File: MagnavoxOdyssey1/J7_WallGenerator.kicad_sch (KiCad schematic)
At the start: 19 parts

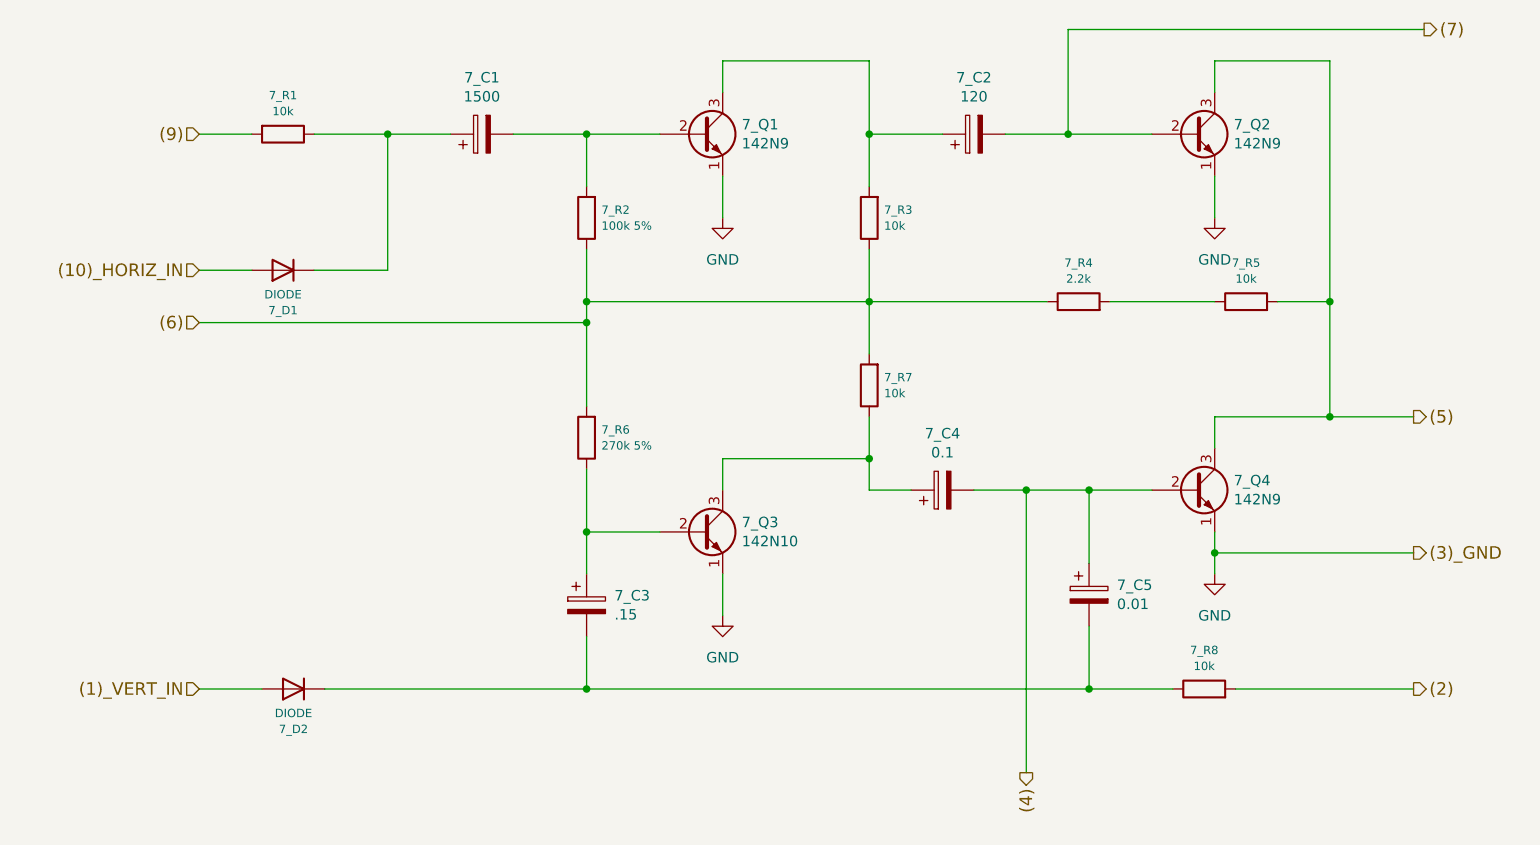
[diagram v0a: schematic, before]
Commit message: update to kicad 9
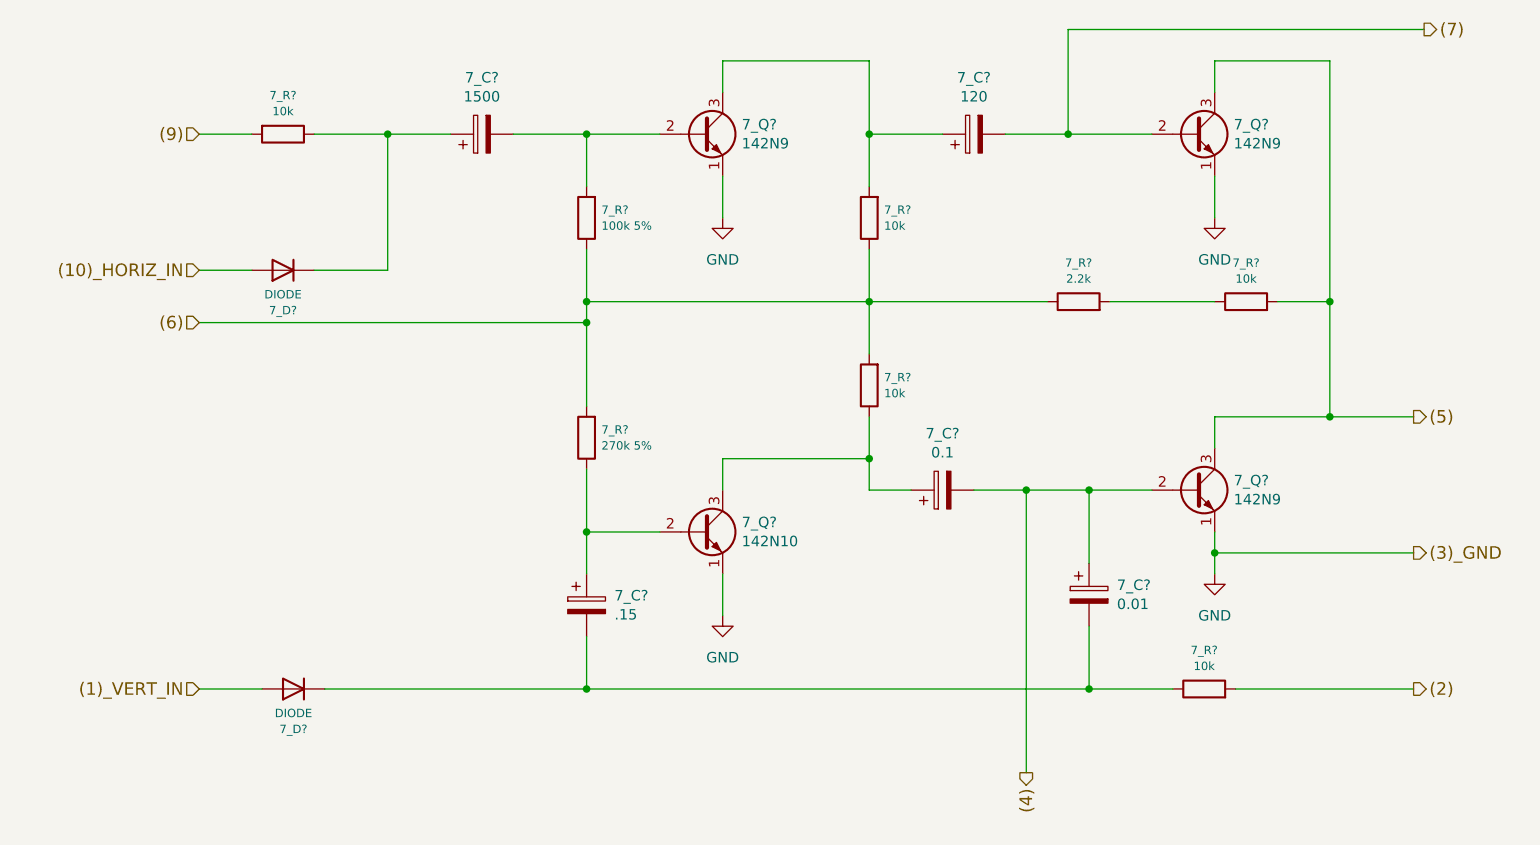
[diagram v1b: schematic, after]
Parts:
- 7_Q?: renamed from 7_Q1; symbol Device:Q_NPN_EBC -> Transistor_BJT:Q_NPN_EBC
- 7_Q?: renamed from 7_Q2; symbol Device:Q_NPN_EBC -> Transistor_BJT:Q_NPN_EBC
- 7_Q?: renamed from 7_Q3; symbol Device:Q_NPN_EBC -> Transistor_BJT:Q_NPN_EBC
- 7_Q?: renamed from 7_Q4; symbol Device:Q_NPN_EBC -> Transistor_BJT:Q_NPN_EBC
- renumbered 7_C1 to 7_C?, 7_C2 to 7_C?, 7_C4 to 7_C?, 7_C5 to 7_C?, 7_C3 to 7_C?, 7_D1 to 7_D?, 7_D2 to 7_D?, 7_R1 to 7_R?, 7_R2 to 7_R?, 7_R3 to 7_R?, 7_R6 to 7_R?, 7_R7 to 7_R?, 7_R8 to 7_R?, 7_R4 to 7_R?, 7_R5 to 7_R?
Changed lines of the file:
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@@
 (kicad_sch
-	(version 20231120)
+	(version 20250114)
 	(generator "eeschema")
-	(generator_version "8.0")
+	(generator_version "9.0")
 	(paper "A4")
 	(junction
@@
 		(on_board yes)
 		(dnp no)
-		(property "Reference" "7_D1"
+		(property "Reference" "7_D?"
 			(at 88.9 84.8868 0)
 			(effects
@@
 		)
 		(pin "1"
+		)
+		(instances
+			(project "MagnavoxOdyssey1"
+				(path "/adb6e295-eae5-402e-a614-02a705c3e27c/00000000-0000-0000-0000-0000588dc7ec"
+					(reference "7_D?")
+					(unit 1)
+				)
+			)
 		)
 	)
@@
 		(on_board yes)
 		(dnp no)
-		(property "Reference" "7_R1"
+		(property "Reference" "7_R?"
 			(at 88.9 58.801 90)
 			(effects
@@
 		)
 		(pin "1"
+		)
+		(instances
+			(project "MagnavoxOdyssey1"
+				(path "/adb6e295-eae5-402e-a614-02a705c3e27c/00000000-0000-0000-0000-0000588dc7ec"
+					(reference "7_R?")
+					(unit 1)
+				)
+			)
 		)
 	)
@@
 		(on_board yes)
 		(dnp no)
-		(property "Reference" "7_C1"
+		(property "Reference" "7_C?"
 			(at 113.03 56.642 90)
 			(effects
@@
 		)
 		(pin "2"
+		)
+		(instances
+			(project "MagnavoxOdyssey1"
+				(path "/adb6e295-eae5-402e-a614-02a705c3e27c/00000000-0000-0000-0000-0000588dc7ec"
+					(reference "7_C?")
+					(unit 1)
+				)
+			)
 		)
 	)
@@
 		(on_board yes)
 		(dnp no)
-		(property "Reference" "7_R2"
+		(property "Reference" "7_R?"
 			(at 127.5334 72.6948 0)
 			(effects
@@
 		(pin "1"
 		)
+		(instances
+			(project "MagnavoxOdyssey1"
+				(path "/adb6e295-eae5-402e-a614-02a705c3e27c/00000000-0000-0000-0000-0000588dc7ec"
+					(reference "7_R?")
+					(unit 1)
+				)
+			)
+		)
 	)
 	(symbol
-		(lib_id "Device:Q_NPN_EBC")
+		(lib_id "Transistor_BJT:Q_NPN_EBC")
 		(at 139.7 63.5 0)
 		(unit 1)
@@
 		(on_board yes)
 		(dnp no)
-		(property "Reference" "7_Q1"
+		(property "Reference" "7_Q?"
 			(at 144.5514 62.3316 0)
 			(effects
@@
 		)
 		(pin "3"
+		)
+		(instances
+			(project "MagnavoxOdyssey1"
+				(path "/adb6e295-eae5-402e-a614-02a705c3e27c/00000000-0000-0000-0000-0000588dc7ec"
+					(reference "7_Q?")
+					(unit 1)
+				)
+			)
 		)
 	)
@@
 		(on_board yes)
 		(dnp no)
-		(property "Reference" "7_R3"
+		(property "Reference" "7_R?"
 			(at 161.8234 72.6948 0)
 			(effects
@@
 		)
 		(pin "2"
+		)
+		(instances
+			(project "MagnavoxOdyssey1"
+				(path "/adb6e295-eae5-402e-a614-02a705c3e27c/00000000-0000-0000-0000-0000588dc7ec"
+					(reference "7_R?")
+					(unit 1)
+				)
+			)
 		)
 	)
@@
 		(on_board yes)
 		(dnp no)
-		(property "Reference" "7_C2"
+		(property "Reference" "7_C?"
 			(at 172.72 56.642 90)
 			(effects
@@
 		(pin "2"
 		)
+		(instances
+			(project "MagnavoxOdyssey1"
+				(path "/adb6e295-eae5-402e-a614-02a705c3e27c/00000000-0000-0000-0000-0000588dc7ec"
+					(reference "7_C?")
+					(unit 1)
+				)
+			)
+		)
 	)
 	(symbol
-		(lib_id "Device:Q_NPN_EBC")
+		(lib_id "Transistor_BJT:Q_NPN_EBC")
 		(at 199.39 63.5 0)
 		(unit 1)
@@
 		(on_board yes)
 		(dnp no)
-		(property "Reference" "7_Q2"
+		(property "Reference" "7_Q?"
 			(at 204.2414 62.3316 0)
 			(effects
@@
 		)
 		(pin "3"
+		)
+		(instances
+			(project "MagnavoxOdyssey1"
+				(path "/adb6e295-eae5-402e-a614-02a705c3e27c/00000000-0000-0000-0000-0000588dc7ec"
+					(reference "7_Q?")
+					(unit 1)
+				)
+			)
 		)
 	)
@@
 		(on_board yes)
 		(dnp no)
-		(property "Reference" "7_R6"
+		(property "Reference" "7_R?"
 			(at 127.5334 99.3648 0)
 			(effects
@@
 		(pin "2"
 		)
+		(instances
+			(project "MagnavoxOdyssey1"
+				(path "/adb6e295-eae5-402e-a614-02a705c3e27c/00000000-0000-0000-0000-0000588dc7ec"
+					(reference "7_R?")
+					(unit 1)
+				)
+			)
+		)
 	)
 	(symbol
-		(lib_id "Device:Q_NPN_EBC")
+		(lib_id "Transistor_BJT:Q_NPN_EBC")
 		(at 139.7 111.76 0)
 		(unit 1)
@@
 		(on_board yes)
 		(dnp no)
-		(property "Reference" "7_Q3"
+		(property "Reference" "7_Q?"
 			(at 144.5514 110.5916 0)
 			(effects
@@
 		)
 		(pin "3"
+		)
+		(instances
+			(project "MagnavoxOdyssey1"
+				(path "/adb6e295-eae5-402e-a614-02a705c3e27c/00000000-0000-0000-0000-0000588dc7ec"
+					(reference "7_Q?")
+					(unit 1)
+				)
+			)
 		)
 	)
@@
 		(on_board yes)
 		(dnp no)
-		(property "Reference" "7_R7"
+		(property "Reference" "7_R?"
 			(at 161.8234 93.0148 0)
 			(effects
@@
 		)
 		(pin "2"
+		)
+		(instances
+			(project "MagnavoxOdyssey1"
+				(path "/adb6e295-eae5-402e-a614-02a705c3e27c/00000000-0000-0000-0000-0000588dc7ec"
+					(reference "7_R?")
+					(unit 1)
+				)
+			)
 		)
 	)
@@
 		(on_board yes)
 		(dnp no)
-		(property "Reference" "7_C4"
+		(property "Reference" "7_C?"
 			(at 168.91 99.822 90)
 			(effects
@@
 		)
 		(pin "2"
+		)
+		(instances
+			(project "MagnavoxOdyssey1"
+				(path "/adb6e295-eae5-402e-a614-02a705c3e27c/00000000-0000-0000-0000-0000588dc7ec"
+					(reference "7_C?")
+					(unit 1)
+				)
+			)
 		)
 	)
@@
 		(on_board yes)
 		(dnp no)
-		(property "Reference" "7_C5"
+		(property "Reference" "7_C?"
 			(at 190.0682 118.2116 0)
 			(effects
@@
 		)
 		(pin "2"
+		)
+		(instances
+			(project "MagnavoxOdyssey1"
+				(path "/adb6e295-eae5-402e-a614-02a705c3e27c/00000000-0000-0000-0000-0000588dc7ec"
+					(reference "7_C?")
+					(unit 1)
+				)
+			)
 		)
 	)
@@
 		(on_board yes)
 		(dnp no)
-		(property "Reference" "7_C3"
+		(property "Reference" "7_C?"
 			(at 129.1082 119.4816 0)
 			(effects
@@
 		)
 		(pin "2"
+		)
+		(instances
+			(project "MagnavoxOdyssey1"
+				(path "/adb6e295-eae5-402e-a614-02a705c3e27c/00000000-0000-0000-0000-0000588dc7ec"
+					(reference "7_C?")
+					(unit 1)
+				)
+			)
 		)
 	)
@@
 		(on_board yes)
 		(dnp no)
-		(property "Reference" "7_R8"
+		(property "Reference" "7_R?"
 			(at 200.66 126.111 90)
 			(effects
@@
 		(pin "2"
 		)
+		(instances
+			(project "MagnavoxOdyssey1"
+				(path "/adb6e295-eae5-402e-a614-02a705c3e27c/00000000-0000-0000-0000-0000588dc7ec"
+					(reference "7_R?")
+					(unit 1)
+				)
+			)
+		)
 	)
 	(symbol
-		(lib_id "Device:Q_NPN_EBC")
+		(lib_id "Transistor_BJT:Q_NPN_EBC")
 		(at 199.39 106.68 0)
 		(unit 1)
@@
 		(on_board yes)
 		(dnp no)
-		(property "Reference" "7_Q4"
+		(property "Reference" "7_Q?"
 			(at 204.2414 105.5116 0)
 			(effects
@@
 		)
 		(pin "3"
+		)
+		(instances
+			(project "MagnavoxOdyssey1"
+				(path "/adb6e295-eae5-402e-a614-02a705c3e27c/00000000-0000-0000-0000-0000588dc7ec"
+					(reference "7_Q?")
+					(unit 1)
+				)
+			)
 		)
 	)
@@
 		(on_board yes)
 		(dnp no)
-		(property "Reference" "7_R4"
+		(property "Reference" "7_R?"
 			(at 185.42 79.121 90)
 			(effects
@@
 		)
 		(pin "2"
+		)
+		(instances
+			(project "MagnavoxOdyssey1"
+				(path "/adb6e295-eae5-402e-a614-02a705c3e27c/00000000-0000-0000-0000-0000588dc7ec"
+					(reference "7_R?")
+					(unit 1)
+				)
+			)
 		)
 	)
@@
 		(on_board yes)
 		(dnp no)
-		(property "Reference" "7_R5"
+		(property "Reference" "7_R?"
 			(at 205.74 79.121 90)
 			(effects
@@
 		)
 		(pin "2"
+		)
+		(instances
+			(project "MagnavoxOdyssey1"
+				(path "/adb6e295-eae5-402e-a614-02a705c3e27c/00000000-0000-0000-0000-0000588dc7ec"
+					(reference "7_R?")
+					(unit 1)
+				)
+			)
 		)
 	)
@@
 		(on_board yes)
 		(dnp no)
-		(property "Reference" "7_D2"
+		(property "Reference" "7_D?"
 			(at 90.17 135.6868 0)
 			(effects
@@
 		(pin "2"
 		)
-	)
+		(instances
+			(project "MagnavoxOdyssey1"
+				(path "/adb6e295-eae5-402e-a614-02a705c3e27c/00000000-0000-0000-0000-0000588dc7ec"
+					(reference "7_D?")
+					(unit 1)
+				)
+			)
+		)
+	)

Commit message: annotate
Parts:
- gave numbers to parts that had none: 19
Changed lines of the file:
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@@
 		(on_board yes)
 		(dnp no)
-		(property "Reference" "7_D?"
+		(property "Reference" "7_D1"
 			(at 88.9 84.8868 0)
 			(effects
@@
 			(project "MagnavoxOdyssey1"
 				(path "/adb6e295-eae5-402e-a614-02a705c3e27c/00000000-0000-0000-0000-0000588dc7ec"
-					(reference "7_D?")
+					(reference "7_D1")
 					(unit 1)
 				)
@@
 		(on_board yes)
 		(dnp no)
-		(property "Reference" "7_R?"
+		(property "Reference" "7_R1"
 			(at 88.9 58.801 90)
 			(effects
@@
 			(project "MagnavoxOdyssey1"
 				(path "/adb6e295-eae5-402e-a614-02a705c3e27c/00000000-0000-0000-0000-0000588dc7ec"
-					(reference "7_R?")
+					(reference "7_R1")
 					(unit 1)
 				)
@@
 		(on_board yes)
 		(dnp no)
-		(property "Reference" "7_C?"
+		(property "Reference" "7_C1"
 			(at 113.03 56.642 90)
 			(effects
@@
 			(project "MagnavoxOdyssey1"
 				(path "/adb6e295-eae5-402e-a614-02a705c3e27c/00000000-0000-0000-0000-0000588dc7ec"
-					(reference "7_C?")
+					(reference "7_C1")
 					(unit 1)
 				)
@@
 		(on_board yes)
 		(dnp no)
-		(property "Reference" "7_R?"
+		(property "Reference" "7_R2"
 			(at 127.5334 72.6948 0)
 			(effects
@@
 			(project "MagnavoxOdyssey1"
 				(path "/adb6e295-eae5-402e-a614-02a705c3e27c/00000000-0000-0000-0000-0000588dc7ec"
-					(reference "7_R?")
+					(reference "7_R2")
 					(unit 1)
 				)
@@
 		(on_board yes)
 		(dnp no)
-		(property "Reference" "7_Q?"
+		(property "Reference" "7_Q1"
 			(at 144.5514 62.3316 0)
 			(effects
@@
 			(project "MagnavoxOdyssey1"
 				(path "/adb6e295-eae5-402e-a614-02a705c3e27c/00000000-0000-0000-0000-0000588dc7ec"
-					(reference "7_Q?")
+					(reference "7_Q1")
 					(unit 1)
 				)
@@
 		(on_board yes)
 		(dnp no)
-		(property "Reference" "7_R?"
+		(property "Reference" "7_R3"
 			(at 161.8234 72.6948 0)
 			(effects
@@
 			(project "MagnavoxOdyssey1"
 				(path "/adb6e295-eae5-402e-a614-02a705c3e27c/00000000-0000-0000-0000-0000588dc7ec"
-					(reference "7_R?")
+					(reference "7_R3")
 					(unit 1)
 				)
@@
 		(on_board yes)
 		(dnp no)
-		(property "Reference" "7_C?"
+		(property "Reference" "7_C2"
 			(at 172.72 56.642 90)
 			(effects
@@
 			(project "MagnavoxOdyssey1"
 				(path "/adb6e295-eae5-402e-a614-02a705c3e27c/00000000-0000-0000-0000-0000588dc7ec"
-					(reference "7_C?")
+					(reference "7_C2")
 					(unit 1)
 				)
@@
 		(on_board yes)
 		(dnp no)
-		(property "Reference" "7_Q?"
+		(property "Reference" "7_Q2"
 			(at 204.2414 62.3316 0)
 			(effects
@@
 			(project "MagnavoxOdyssey1"
 				(path "/adb6e295-eae5-402e-a614-02a705c3e27c/00000000-0000-0000-0000-0000588dc7ec"
-					(reference "7_Q?")
+					(reference "7_Q2")
 					(unit 1)
 				)
@@
 		(on_board yes)
 		(dnp no)
-		(property "Reference" "7_R?"
+		(property "Reference" "7_R7"
 			(at 127.5334 99.3648 0)
 			(effects
@@
 			(project "MagnavoxOdyssey1"
 				(path "/adb6e295-eae5-402e-a614-02a705c3e27c/00000000-0000-0000-0000-0000588dc7ec"
-					(reference "7_R?")
+					(reference "7_R7")
 					(unit 1)
 				)
@@
 		(on_board yes)
 		(dnp no)
-		(property "Reference" "7_Q?"
+		(property "Reference" "7_Q4"
 			(at 144.5514 110.5916 0)
 			(effects
@@
 			(project "MagnavoxOdyssey1"
 				(path "/adb6e295-eae5-402e-a614-02a705c3e27c/00000000-0000-0000-0000-0000588dc7ec"
-					(reference "7_Q?")
+					(reference "7_Q4")
 					(unit 1)
 				)
@@
 		(on_board yes)
 		(dnp no)
-		(property "Reference" "7_R?"
+		(property "Reference" "7_R6"
 			(at 161.8234 93.0148 0)
 			(effects
@@
 			(project "MagnavoxOdyssey1"
 				(path "/adb6e295-eae5-402e-a614-02a705c3e27c/00000000-0000-0000-0000-0000588dc7ec"
-					(reference "7_R?")
+					(reference "7_R6")
 					(unit 1)
 				)
@@
 		(on_board yes)
 		(dnp no)
-		(property "Reference" "7_C?"
+		(property "Reference" "7_C3"
 			(at 168.91 99.822 90)
 			(effects
@@
 			(project "MagnavoxOdyssey1"
 				(path "/adb6e295-eae5-402e-a614-02a705c3e27c/00000000-0000-0000-0000-0000588dc7ec"
-					(reference "7_C?")
+					(reference "7_C3")
 					(unit 1)
 				)
@@
 		(on_board yes)
 		(dnp no)
-		(property "Reference" "7_C?"
+		(property "Reference" "7_C4"
 			(at 190.0682 118.2116 0)
 			(effects
@@
 			(project "MagnavoxOdyssey1"
 				(path "/adb6e295-eae5-402e-a614-02a705c3e27c/00000000-0000-0000-0000-0000588dc7ec"
-					(reference "7_C?")
+					(reference "7_C4")
 					(unit 1)
 				)
@@
 		(on_board yes)
 		(dnp no)
-		(property "Reference" "7_C?"
+		(property "Reference" "7_C5"
 			(at 129.1082 119.4816 0)
 			(effects
@@
 			(project "MagnavoxOdyssey1"
 				(path "/adb6e295-eae5-402e-a614-02a705c3e27c/00000000-0000-0000-0000-0000588dc7ec"
-					(reference "7_C?")
+					(reference "7_C5")
 					(unit 1)
 				)
@@
 		(on_board yes)
 		(dnp no)
-		(property "Reference" "7_R?"
+		(property "Reference" "7_R8"
 			(at 200.66 126.111 90)
 			(effects
@@
 			(project "MagnavoxOdyssey1"
 				(path "/adb6e295-eae5-402e-a614-02a705c3e27c/00000000-0000-0000-0000-0000588dc7ec"
-					(reference "7_R?")
+					(reference "7_R8")
 					(unit 1)
 				)
@@
 		(on_board yes)
 		(dnp no)
-		(property "Reference" "7_Q?"
+		(property "Reference" "7_Q3"
 			(at 204.2414 105.5116 0)
 			(effects
@@
 			(project "MagnavoxOdyssey1"
 				(path "/adb6e295-eae5-402e-a614-02a705c3e27c/00000000-0000-0000-0000-0000588dc7ec"
-					(reference "7_Q?")
+					(reference "7_Q3")
 					(unit 1)
 				)
@@
 		(on_board yes)
 		(dnp no)
-		(property "Reference" "7_R?"
+		(property "Reference" "7_R4"
 			(at 185.42 79.121 90)
 			(effects
@@
 			(project "MagnavoxOdyssey1"
 				(path "/adb6e295-eae5-402e-a614-02a705c3e27c/00000000-0000-0000-0000-0000588dc7ec"
-					(reference "7_R?")
+					(reference "7_R4")
 					(unit 1)
 				)
@@
 		(on_board yes)
 		(dnp no)
-		(property "Reference" "7_R?"
+		(property "Reference" "7_R5"
 			(at 205.74 79.121 90)
 			(effects
@@
 			(project "MagnavoxOdyssey1"
 				(path "/adb6e295-eae5-402e-a614-02a705c3e27c/00000000-0000-0000-0000-0000588dc7ec"
-					(reference "7_R?")
+					(reference "7_R5")
 					(unit 1)
 				)
@@
 		(on_board yes)
 		(dnp no)
-		(property "Reference" "7_D?"
+		(property "Reference" "7_D2"
 			(at 90.17 135.6868 0)
 			(effects
@@
 			(project "MagnavoxOdyssey1"
 				(path "/adb6e295-eae5-402e-a614-02a705c3e27c/00000000-0000-0000-0000-0000588dc7ec"
-					(reference "7_D?")
-					(unit 1)
-				)
+					(reference "7_D2")
+					(unit 1)
+				)

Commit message: accurate resistors
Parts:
- 7_R2: value 100k 5% -> 100k
- 7_R7: value 270k 5% -> 270k
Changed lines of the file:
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@@
 			)
 		)
-		(property "Value" "100k 5%"
+		(property "Value" "100k"
 			(at 127.5334 74.6252 0)
 			(effects
@@
 			)
 		)
-		(property "Value" "270k 5%"
+		(property "Value" "270k"
 			(at 127.5334 101.2952 0)
 			(effects
